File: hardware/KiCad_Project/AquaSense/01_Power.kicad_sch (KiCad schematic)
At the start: 3 parts, among them J1 USB_C_Receptacle_USB2.0_16P

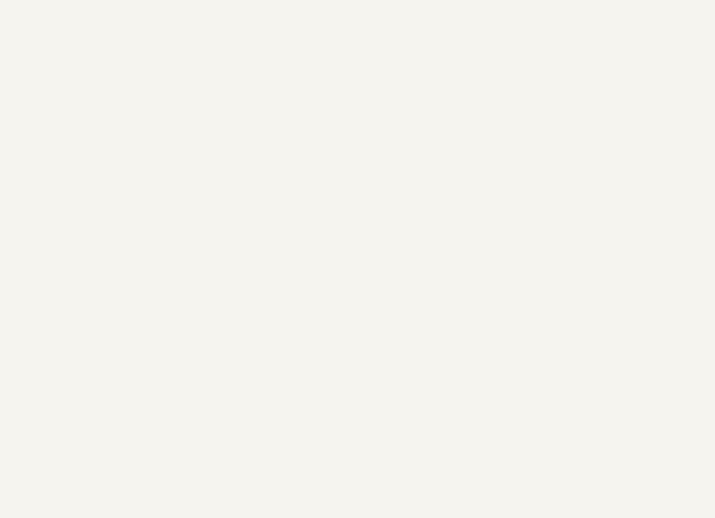
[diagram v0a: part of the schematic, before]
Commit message: Complete core power architecture for AquaSense
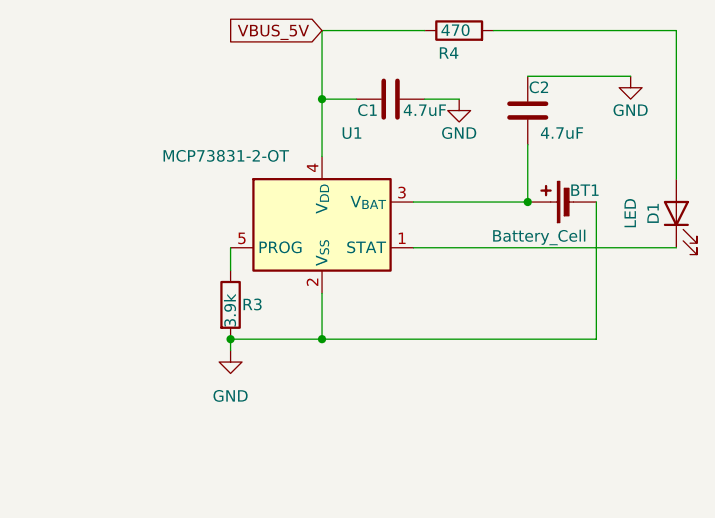
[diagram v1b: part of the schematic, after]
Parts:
- added BT1: Battery_Cell, symbol Device:Battery_Cell
- added C1, C2: 4.7uF, symbol Device:C
- added D1: LED, symbol Device:LED
- added R3: 3.9k, symbol Device:R
- added R4: 470, symbol Device:R
- added U1: MCP73831-2-OT, Package_TO_SOT_SMD:SOT-23-5, symbol Battery_Management:MCP73831-2-OT
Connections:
- net GND: now also BT1.2 (-), C1.2, C2.2, R3.2, U1.2 (V_{SS})
- net VBUS_5V: now also C1.1, R4.1, U1.4 (V_{DD})
- new net: D1.1 (K), U1.1 (STAT)
- new net: D1.2 (A), R4.2
- new net: BT1.1 (+), C2.1, U1.3 (V_{BAT})
- new net: R3.1, U1.5 (PROG)

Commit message: Completed power route
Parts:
- added C3, C4: 10uF, symbol Device:C
- added U2: MCP1700x-330xxTT, Package_TO_SOT_SMD:SOT-23, symbol Regulator_Linear:MCP1700x-330xxTT
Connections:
- net GND: now also C4.2
- new net: C3.2, U2.3 (VI)
- new net VBAT: C3.1
- new net VCC_3V3: C4.1, U2.2 (VO)
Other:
- note added: "BATTERY CHARGER"
- note added: "USB INPUT"
- note added: "VOLTAGE REGULATION"
- moved on the sheet: BT1, C1, C2, D1, R3, R4, U1
